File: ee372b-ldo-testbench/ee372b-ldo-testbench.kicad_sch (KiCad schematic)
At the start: 136 parts, among them J1 PEC02SAAN, J10 OUT_S, J11 VOUT, J12 VDD_BUF, J13 V_SIG, J14 PEC03SAAN, J15 VSIG_BUF, J16 PEC03SAAN, J17 PEC03SAAN, J18 PEC03SAAN, J19 PEC03SAAN, J2 PEC02SAAN, J20 VREF_EXTERNAL, J21 PEC02SAAN, J22 PEC02SAAN, J23 PEC02SAAN, J24 PEC02SAAN, J25 PEC03SAAN, J3 GND, J4 1V8, J5 3v3_EXTERNAL, J8 VIN, J9 IN_S, Q1 FDV305N, Q2 FDV305N, Q3 FDV305N, Q4 FDV305N, Q5 FDV305N, U1 MMSZ4679T1G, U3 ADS1220IPW, U4 BUF634AIDR

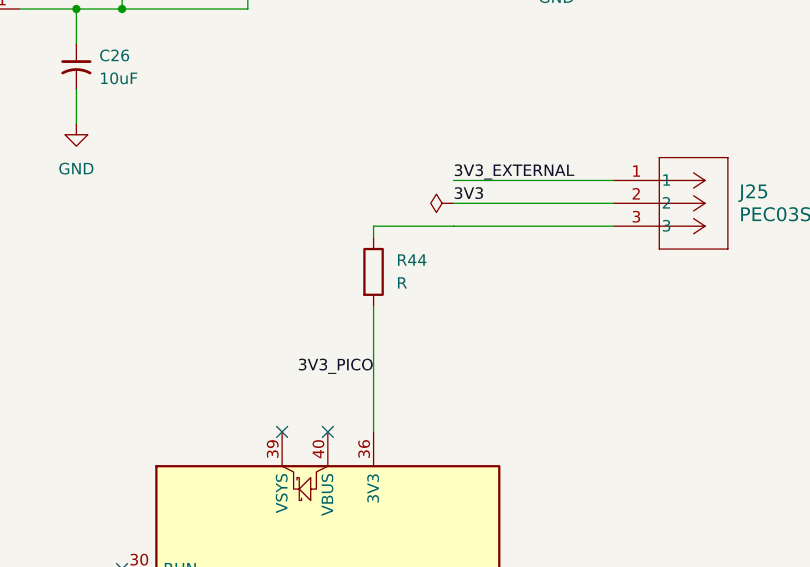
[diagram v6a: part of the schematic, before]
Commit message: adding footprints
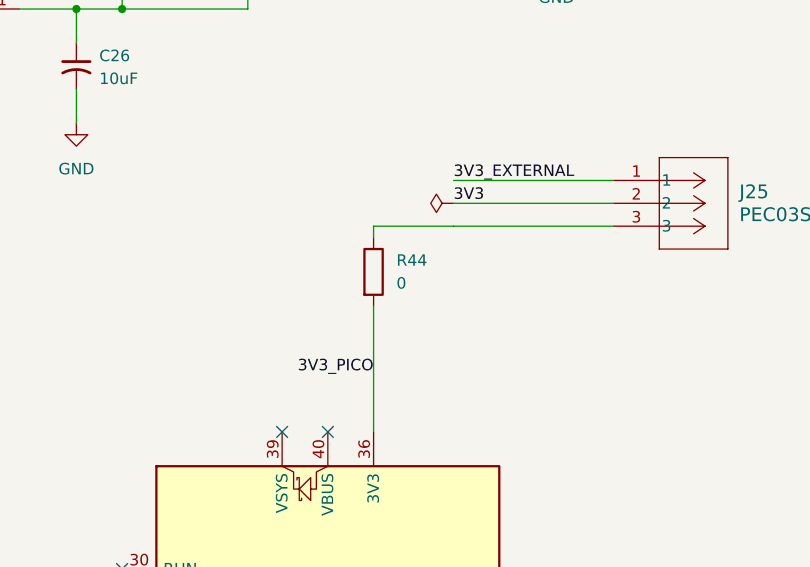
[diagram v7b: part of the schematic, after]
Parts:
- C10, C17, C23, C24, C26, C27, C28, C4, C5, C6, C7, C9: footprint (none) -> Capacitor_SMD:C_0805_2012Metric_Pad1.18x1.45mm_HandSolder
- R44: value R -> 0; footprint (none) -> Resistor_SMD:R_0805_2012Metric_Pad1.20x1.40mm_HandSolder
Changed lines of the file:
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@@
 			)
 		)
-		(property "Footprint" ""
+		(property "Footprint" "Capacitor_SMD:C_0805_2012Metric_Pad1.18x1.45mm_HandSolder"
 			(at 372.11 73.66 0)
 			(hide yes)
@@
 			)
 		)
-		(property "Footprint" ""
+		(property "Footprint" "Capacitor_SMD:C_0805_2012Metric_Pad1.18x1.45mm_HandSolder"
 			(at 204.47 227.33 0)
 			(hide yes)
@@
 			)
 		)
-		(property "Value" "R"
+		(property "Value" "0"
 			(at 240.03 251.4599 0)
 			(show_name no)
@@
 			)
 		)
-		(property "Footprint" ""
+		(property "Footprint" "Resistor_SMD:R_0805_2012Metric_Pad1.20x1.40mm_HandSolder"
 			(at 235.712 250.19 90)
 			(hide yes)
@@
 			)
 		)
-		(property "Footprint" ""
+		(property "Footprint" "Capacitor_SMD:C_0805_2012Metric_Pad1.18x1.45mm_HandSolder"
 			(at 257.81 208.28 0)
 			(hide yes)
@@
 			)
 		)
-		(property "Footprint" ""
+		(property "Footprint" "Capacitor_SMD:C_0805_2012Metric_Pad1.18x1.45mm_HandSolder"
 			(at 367.03 73.66 0)
 			(hide yes)
@@
 			)
 		)
-		(property "Footprint" ""
+		(property "Footprint" "Capacitor_SMD:C_0805_2012Metric_Pad1.18x1.45mm_HandSolder"
 			(at 361.95 73.66 0)
 			(hide yes)
@@
 			)
 		)
-		(property "Footprint" ""
+		(property "Footprint" "Capacitor_SMD:C_0805_2012Metric_Pad1.18x1.45mm_HandSolder"
 			(at 382.27 73.66 0)
 			(hide yes)
@@
 			)
 		)
-		(property "Footprint" ""
+		(property "Footprint" "Capacitor_SMD:C_0805_2012Metric_Pad1.18x1.45mm_HandSolder"
 			(at 369.57 73.66 0)
 			(hide yes)
@@
 			)
 		)
-		(property "Footprint" ""
+		(property "Footprint" "Capacitor_SMD:C_0805_2012Metric_Pad1.18x1.45mm_HandSolder"
 			(at 374.65 73.66 0)
 			(hide yes)
@@
 			)
 		)
-		(property "Footprint" ""
+		(property "Footprint" "Capacitor_SMD:C_0805_2012Metric_Pad1.18x1.45mm_HandSolder"
 			(at 359.41 73.66 0)
 			(hide yes)
@@
 			)
 		)
-		(property "Footprint" ""
+		(property "Footprint" "Capacitor_SMD:C_0805_2012Metric_Pad1.18x1.45mm_HandSolder"
 			(at 364.49 73.66 0)
 			(hide yes)
@@
 			)
 		)
-		(property "Footprint" ""
+		(property "Footprint" "Capacitor_SMD:C_0805_2012Metric_Pad1.18x1.45mm_HandSolder"
 			(at 356.87 73.66 0)
 			(hide yes)
@@
 			)
 		)
-		(property "Footprint" ""
+		(property "Footprint" "Capacitor_SMD:C_0805_2012Metric_Pad1.18x1.45mm_HandSolder"
 			(at 354.33 73.66 0)
 			(hide yes)

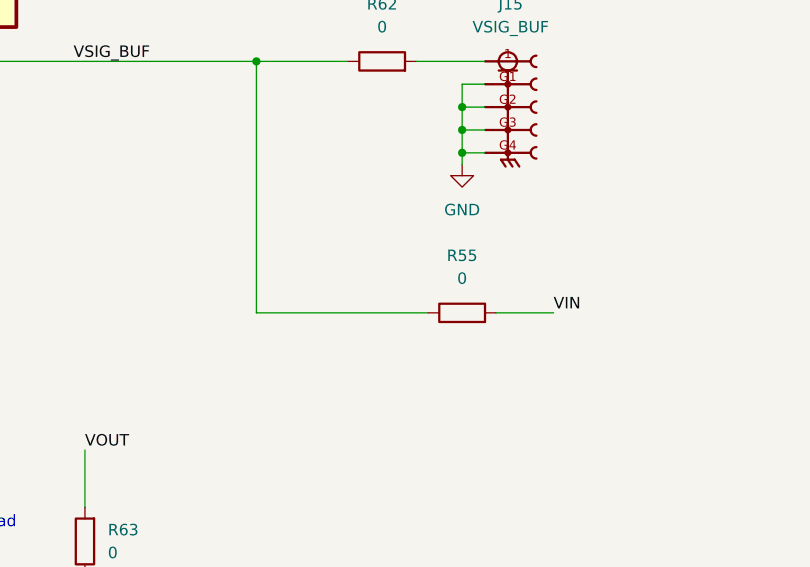
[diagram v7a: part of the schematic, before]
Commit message: updated QFN courtyard
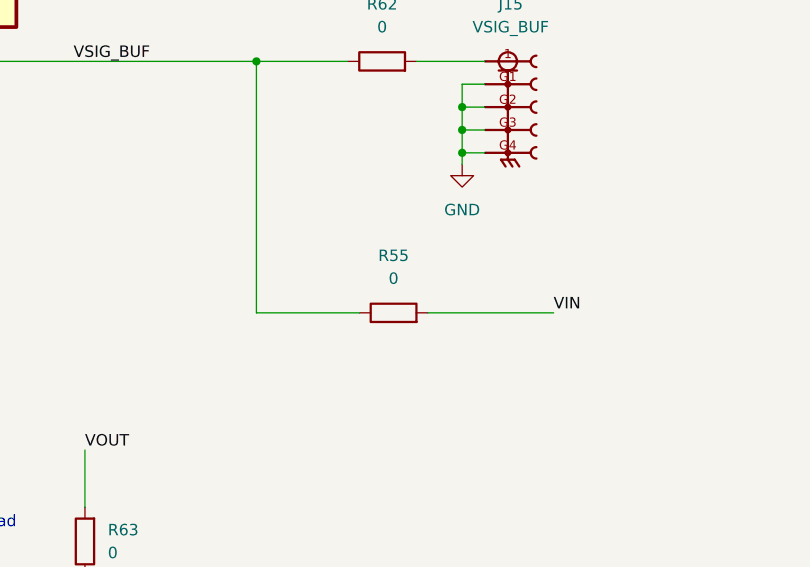
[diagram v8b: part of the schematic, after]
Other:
- moved on the sheet: R55
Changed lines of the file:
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@@
 	(wire
 		(pts
-			(xy 149.86 251.46) (xy 156.21 251.46)
+			(xy 142.24 251.46) (xy 156.21 251.46)
 		)
 		(stroke
@@
 	(wire
 		(pts
-			(xy 123.19 251.46) (xy 142.24 251.46)
+			(xy 123.19 251.46) (xy 134.62 251.46)
 		)
 		(stroke
@@
 	(symbol
 		(lib_id "Device:R")
-		(at 146.05 251.46 90)
+		(at 138.43 251.46 90)
 		(unit 1)
 		(body_style 1)
@@
 		(fields_autoplaced yes)
 		(property "Reference" "R55"
-			(at 146.05 245.11 90)
+			(at 138.43 245.11 90)
 			(show_name no)
 			(do_not_autoplace no)
@@
 		)
 		(property "Value" "0"
-			(at 146.05 247.65 90)
+			(at 138.43 247.65 90)
 			(show_name no)
 			(do_not_autoplace no)
@@
 		)
 		(property "Footprint" "Resistor_SMD:R_0805_2012Metric_Pad1.20x1.40mm_HandSolder"
-			(at 146.05 253.238 90)
+			(at 138.43 253.238 90)
 			(hide yes)
 			(show_name no)
@@
 		)
 		(property "Datasheet" "https://www.vishay.com/docs/20043/crcwhpe3.pdf"
-			(at 146.05 251.46 0)
+			(at 138.43 251.46 0)
 			(hide yes)
 			(show_name no)
@@
 		)
 		(property "Description" "RES SMD 0 OHM JUMPER 1/2W 0805"
-			(at 146.05 251.46 0)
+			(at 138.43 251.46 0)
 			(hide yes)
 			(show_name no)
@@
 		)
 		(property "Manufacturer" "Vishay Dale"
-			(at 146.05 251.46 0)
+			(at 138.43 251.46 0)
 			(hide yes)
 			(show_name no)
@@
 		)
 		(property "Manufacturer Part Number" "CRCW08050000Z0EAHP"
-			(at 146.05 251.46 0)
+			(at 138.43 251.46 0)
 			(hide yes)
 			(show_name no)
@@
 		)
 		(property "Distributer Link 1" "https://www.digikey.com/en/products/detail/vishay-dale/CRCW08050000Z0EAHP/2222316"
-			(at 146.05 251.46 0)
+			(at 138.43 251.46 0)
 			(hide yes)
 			(show_name no)
@@
 		)
 		(property "Distrbuter Link 2" "https://www.mouser.com/en/ProductDetail/Vishay/CRCW08050000Z0EAHP?qs=pTGEtN%252BMLlDLrJUqQmN2jA%3D%3D"
-			(at 146.05 251.46 0)
+			(at 138.43 251.46 0)
 			(hide yes)
 			(show_name no)
